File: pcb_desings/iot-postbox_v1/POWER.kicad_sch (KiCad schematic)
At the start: 32 parts, among them J1 USB_B_Micro, J4 BAT, J5 3V3_LDO2, Q1 AO3401A, U5 MCP73831-2-OT, U6 NCP167BMX330TBG, U7 NCP167BMX330TBG

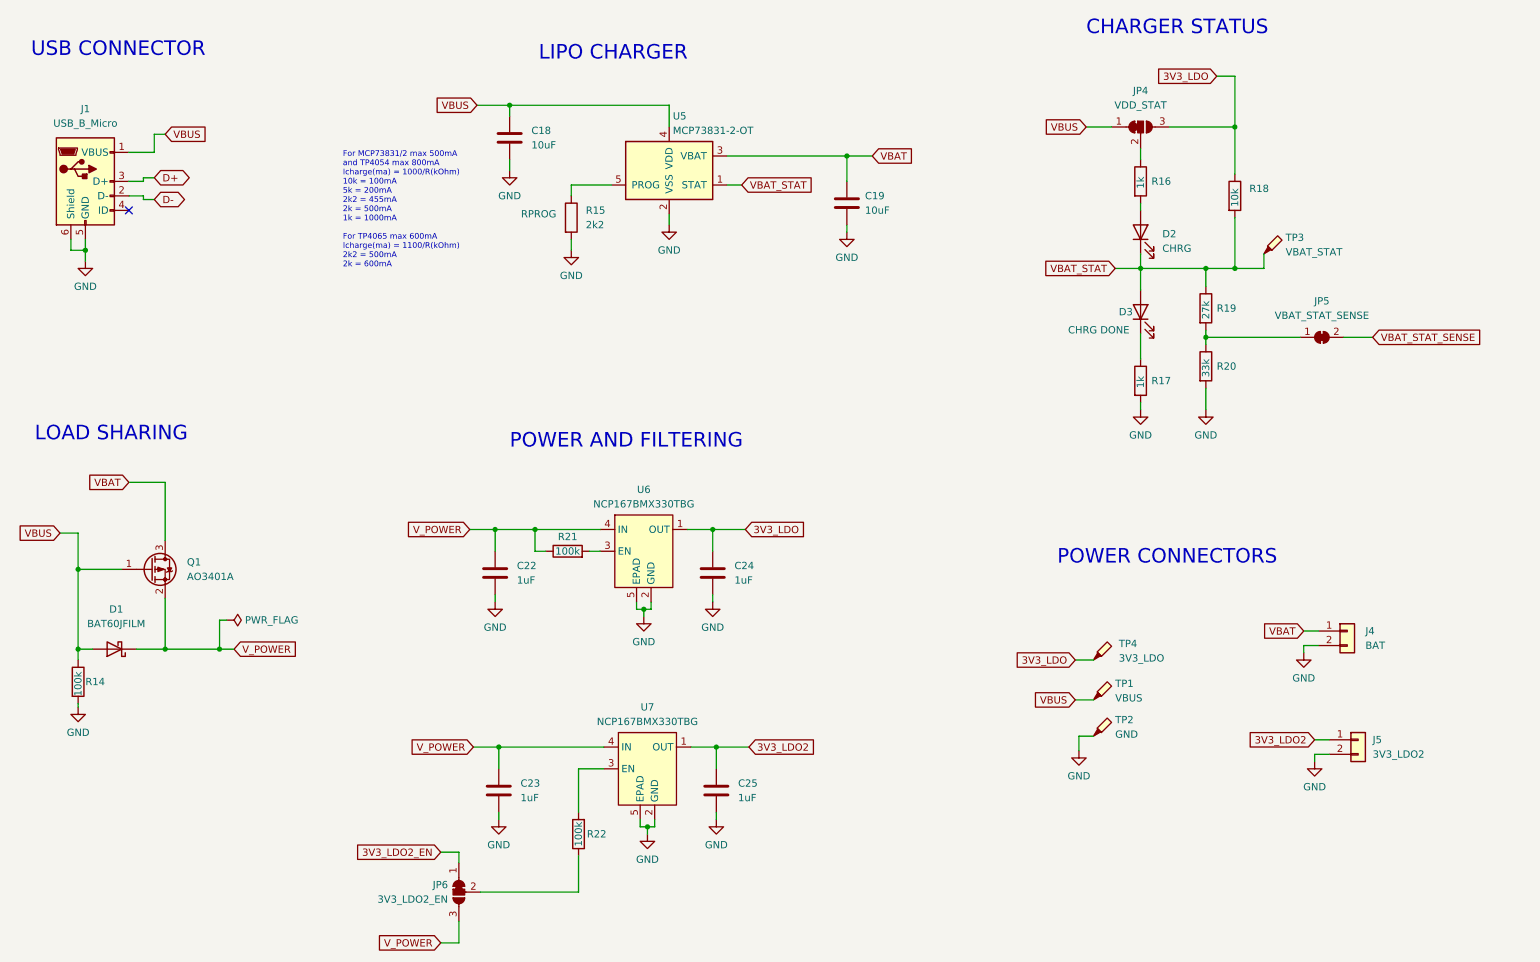
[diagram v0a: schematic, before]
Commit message: Added iot-postbox_v1 sch to v1.1. Added minor documentation
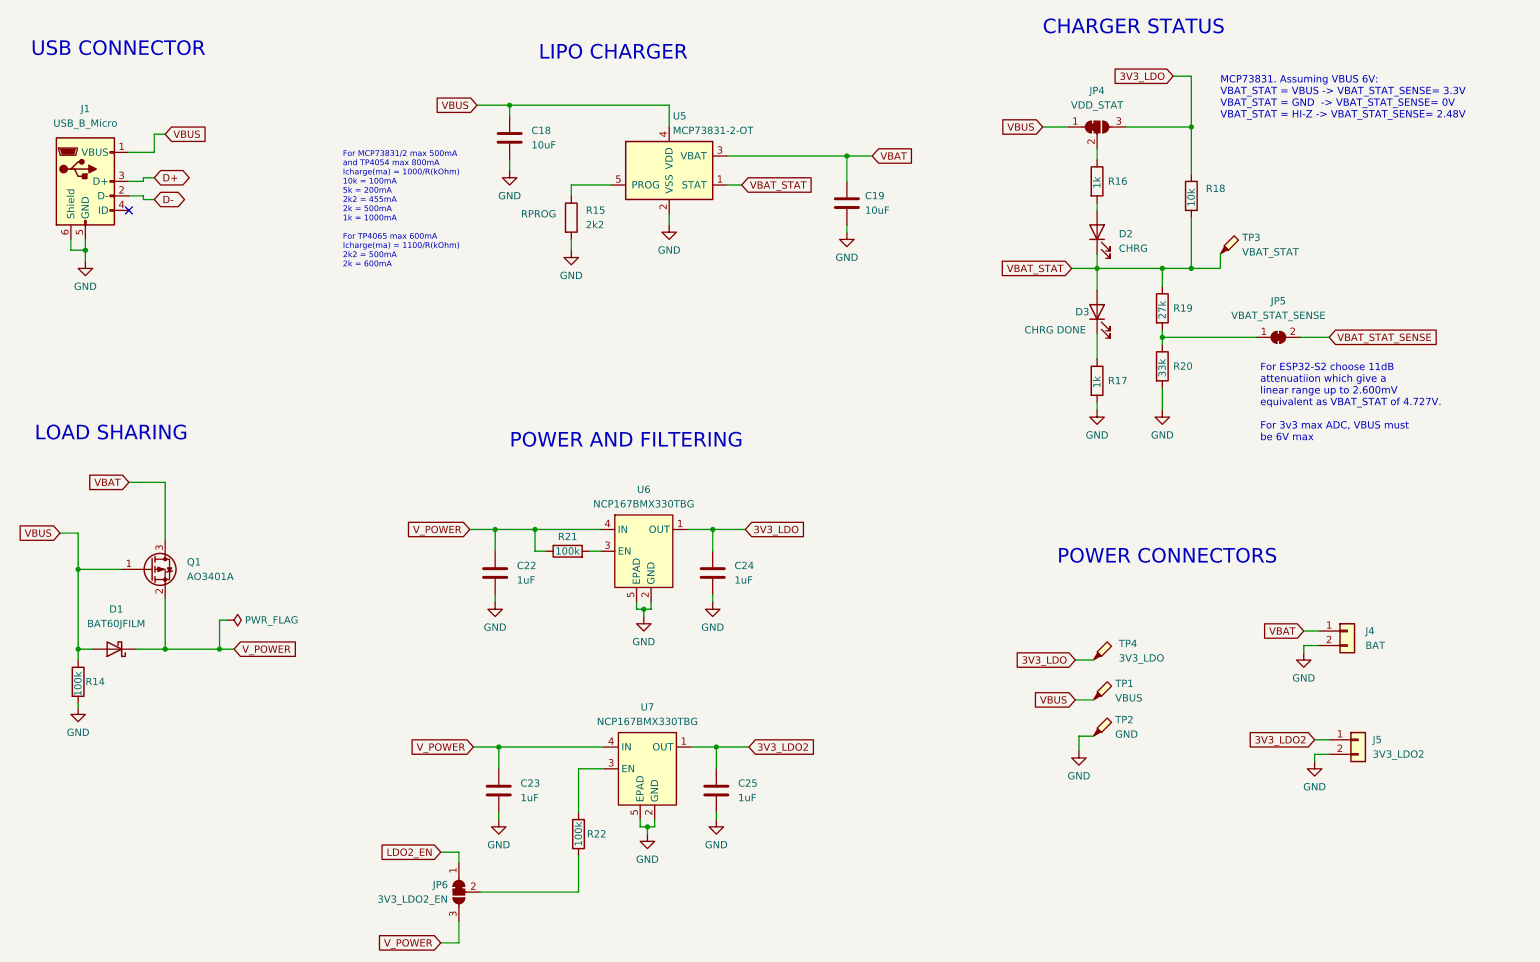
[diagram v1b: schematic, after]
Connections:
- net 3V3_LDO2_EN renamed LDO2_EN
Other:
- note added: "For ESP32-S2 choose 11dB attenuatiion which give a linear range up to 2.600mV equivalent as VBAT_STAT of 4.727V. For 3v3 max ADC, VBUS must be 6V max"
- note added: "MCP73831. Assuming VBUS 6V: VBAT_STAT = VBUS -> VBAT_STAT_SENSE= 3.3V VBAT_STAT = GND -> VBAT_STAT_SENSE= 0V VBAT_STAT = HI-Z -> VBAT_STAT_SENSE= 2.48V"
- moved on the sheet: D2, D3, JP4, JP5, R16, R17, R18, R19, R20, TP3

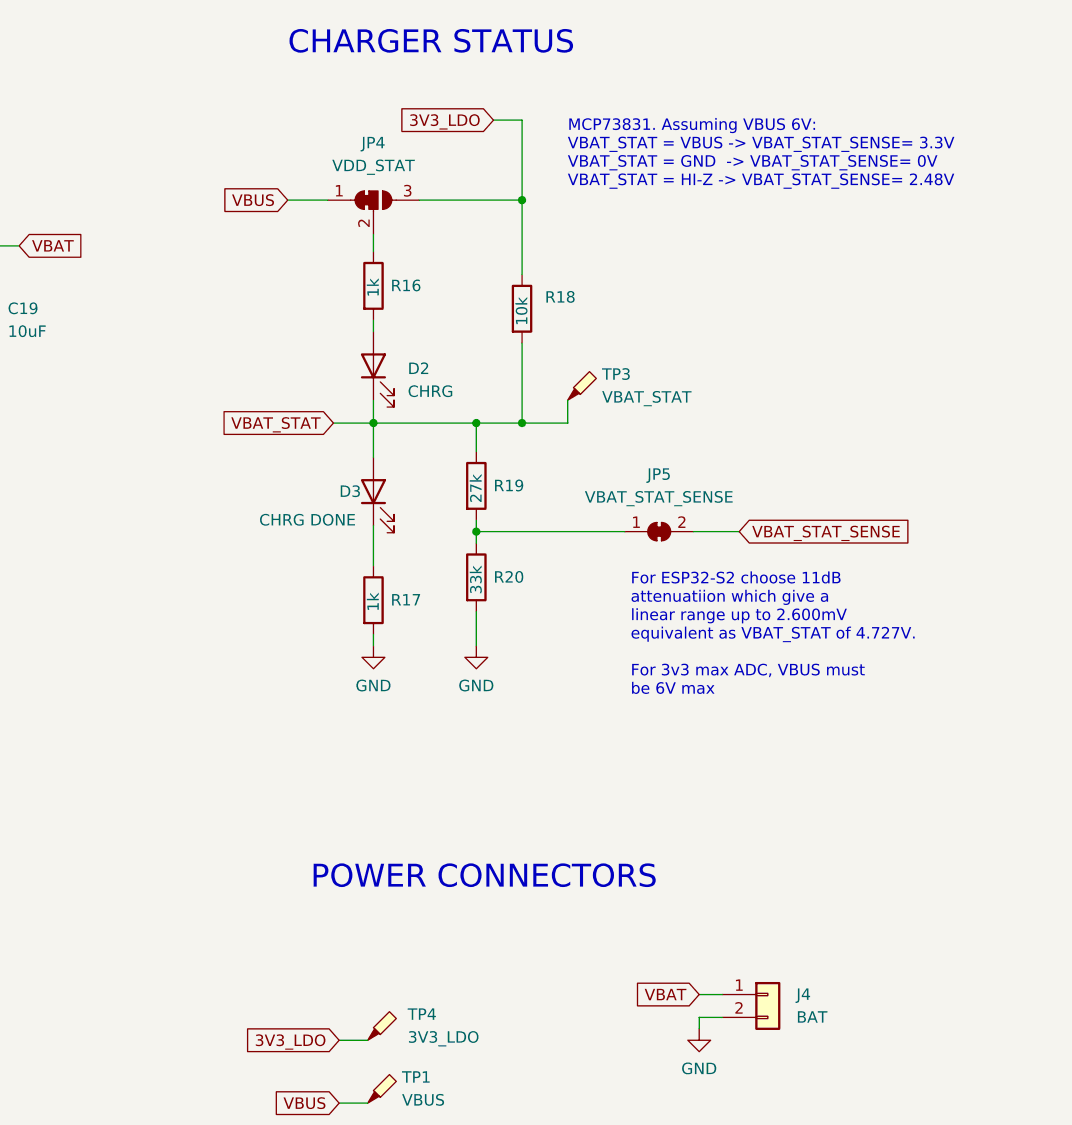
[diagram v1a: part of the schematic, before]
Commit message: Changed led strip instance as fastled object insted adafruit neopixel and fixed power and charging states
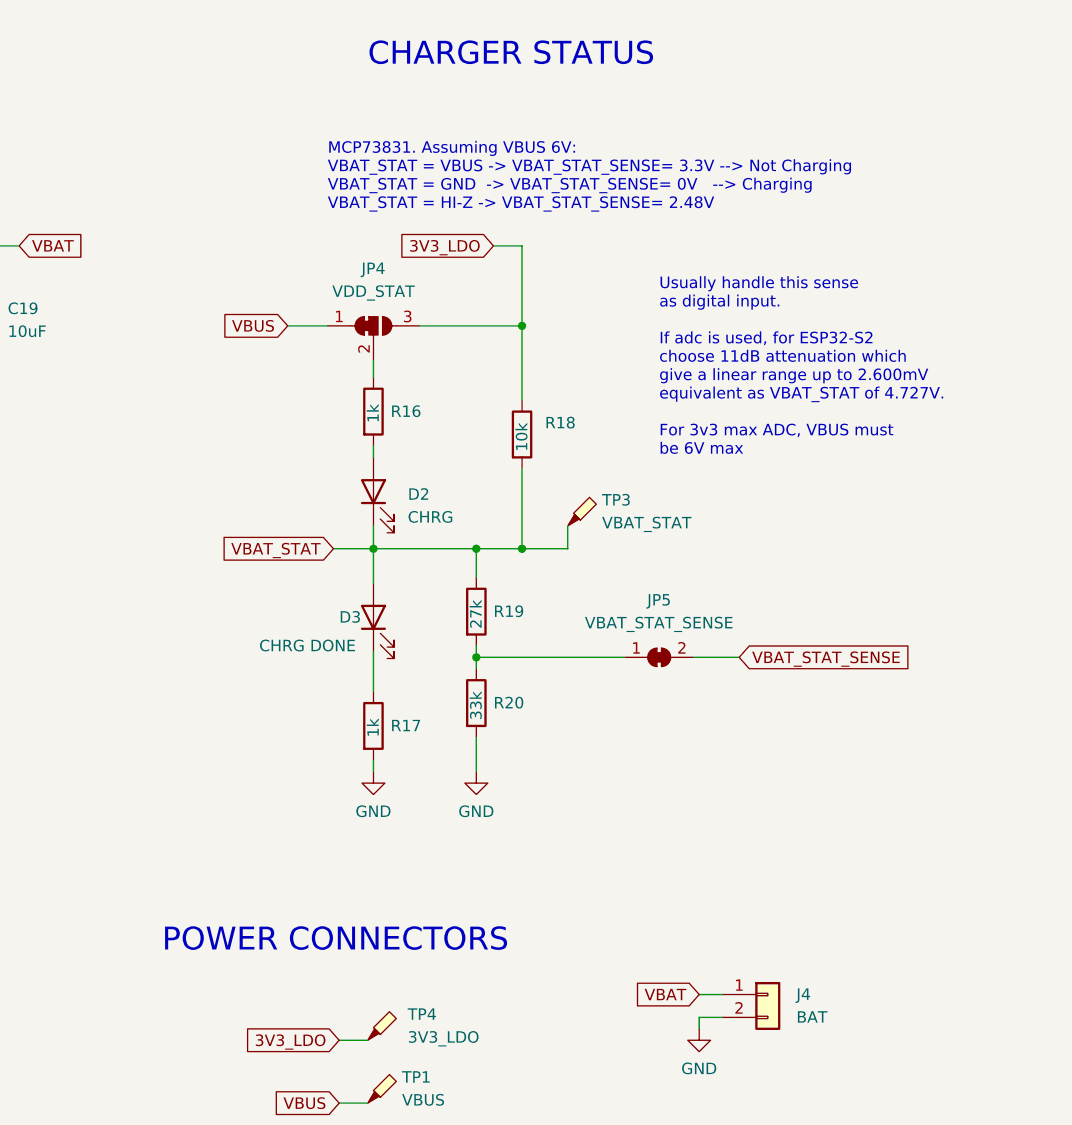
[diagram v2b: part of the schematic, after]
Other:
- note added: "MCP73831. Assuming VBUS 6V: VBAT_STAT = VBUS -> VBAT_STAT_SENSE= 3.3V --> Not Charging VBAT_STAT = GND -> VBAT_STAT_SENSE= 0V --> Charging VBAT_STAT = HI-Z -> VBAT_STAT_SENSE= 2.48V"
- note added: "Usually handle this sense as digital input. If adc is used, for ESP32-S2 choose 11dB attenuation which give a linear range up to 2.600mV equivalent as VBAT_STAT of 4.727V. For 3v3 max ADC, VBUS must be 6V max"
- note removed: "For ESP32-S2 choose 11dB attenuatiion which give a linear range up to 2.600mV equivalent as VBAT_STAT of 4.727V. For 3v3 max ADC, VBUS must be 6V max"
- note removed: "MCP73831. Assuming VBUS 6V: VBAT_STAT = VBUS -> VBAT_STAT_SENSE= 3.3V VBAT_STAT = GND -> VBAT_STAT_SENSE= 0V VBAT_STAT = HI-Z -> VBAT_STAT_SENSE= 2.48V"
- moved on the sheet: D2, D3, JP4, JP5, R16, R17, R18, R19, R20, TP3

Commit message: Added charging circuit test findings
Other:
- note added: "Depending the IC, the VBAT_STAT output can be: - Tri-state output: MCP73831 - Open-drain output: MCP73832, TP4054 or TP4065 Only for Open-drain, R18 make sense because VDD_STAT can be configurable only in that case"
- note added: "For MCP73831/2 max 500mA and TP4054 max 800mA Icharge(ma) = 1000(V)/R(kOhm) 10k = 100mA 5k = 200mA 2k2 = 455mA 2k = 500mA 1k = 1000mA For TP4065 max 600mA Icharge(ma) = 1100/R(kOhm) 2k2 = 500mA 2k = 600mA"
- note removed: "For MCP73831/2 max 500mA and TP4054 max 800mA Icharge(ma) = 1000/R(kOhm) 10k = 100mA 5k = 200mA 2k2 = 455mA 2k = 500mA 1k = 1000mA For TP4065 max 600mA Icharge(ma) = 1100/R(kOhm) 2k2 = 500mA 2k = 600mA"
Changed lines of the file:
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@@
     (effects (font (size 1.27 1.27)) (justify left bottom))
   )
-  (text "For MCP73831/2 max 500mA \nand TP4054 max 800mA\nIcharge(ma) = 1000/R(kOhm)\n10k = 100mA\n5k = 200mA\n2k2 = 455mA\n2k = 500mA\n1k = 1000mA\n\nFor TP4065 max 600mA\nIcharge(ma) = 1100/R(kOhm)\n2k2 = 500mA\n2k = 600mA"
-    (at 80.01 65.405 0)
+  (text "For MCP73831/2 max 500mA \nand TP4054 max 800mA\nIcharge(ma) = 1000(V)/R(kOhm)\n10k = 100mA\n5k = 200mA\n2k2 = 455mA\n2k = 500mA\n1k = 1000mA\n\nFor TP4065 max 600mA\nIcharge(ma) = 1100/R(kOhm)\n2k2 = 500mA\n2k = 600mA"
+    (at 77.47 63.5 0)
     (effects (font (size 1 1)) (justify left bottom))
   )
@@
     (effects (font (size 2.54 2.54)) (justify left bottom))
   )
+  (text "Depending the IC, the VBAT_STAT output can be:\n- Tri-state output: MCP73831\n- Open-drain output: MCP73832, TP4054 or TP4065\nOnly for Open-drain, R18 make sense because \nVDD_STAT can be configurable only in that case"
+    (at 139.7 74.295 0)
+    (effects (font (size 1 1)) (justify left bottom))
+  )
   (text "LIPO CHARGER" (at 114.3 29.21 0)
     (effects (font (size 2.54 2.54)) (justify left bottom))
   )
   (text "MCP73831. Assuming VBUS 6V:\nVBAT_STAT = VBUS -> VBAT_STAT_SENSE= 3.3V --> Not Charging\nVBAT_STAT = GND  -> VBAT_STAT_SENSE= 0V   --> Charging\nVBAT_STAT = HI-Z -> VBAT_STAT_SENSE= 2.48V"
-    (at 207.01 41.91 0)
+    (at 201.93 40.64 0)
     (effects (font (size 1.27 1.27)) (justify left bottom))
   )

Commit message: Added some sch info
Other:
- note added: "Protecctions: - Battery and input reverse polarity WARNING: - No temp protection - No Overcurrent protection"
- note added: "Usually handle VBAT_STAT_SENSE as digital input. If ADC is used, for ESP32-S2 choose 11dB attenuation which give a linear range up to 2.600mV equivalent as VBAT_STAT of 4.727V. For 3v3 max ADC, VBUS must be 6V max"
- note removed: "Usually handle this sense as digital input. If adc is used, for ESP32-S2 choose 11dB attenuation which give a linear range up to 2.600mV equivalent as VBAT_STAT of 4.727V. For 3v3 max ADC, VBUS must be 6V max"
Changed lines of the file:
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@@
     (effects (font (size 2.54 2.54)) (justify left bottom))
   )
-  (text "Usually handle this sense \nas digital input.\n\nIf adc is used, for ESP32-S2 \nchoose 11dB attenuation which \ngive a linear range up to 2.600mV\nequivalent as VBAT_STAT of 4.727V.\n\nFor 3v3 max ADC, VBUS must\nbe 6V max "
+  (text "Usually handle VBAT_STAT_SENSE \nas digital input.\n\nIf ADC is used, for ESP32-S2 \nchoose 11dB attenuation which \ngive a linear range up to 2.600mV\nequivalent as VBAT_STAT of 4.727V.\n\nFor 3v3 max ADC, VBUS must\nbe 6V max "
     (at 243.84 69.215 0)
     (effects (font (size 1.27 1.27)) (justify left bottom))
@@
     (effects (font (size 2.54 2.54)) (justify left bottom))
   )
+  (text "Protecctions:\n- Battery and input reverse polarity\nWARNING:\n- No temp protection\n- No Overcurrent protection"
+    (at 151.13 34.29 0)
+    (effects (font (size 1 1)) (justify left bottom))
+  )
   (text "MCP73831. Assuming VBUS 6V:\nVBAT_STAT = VBUS -> VBAT_STAT_SENSE= 3.3V --> Not Charging\nVBAT_STAT = GND  -> VBAT_STAT_SENSE= 0V   --> Charging\nVBAT_STAT = HI-Z -> VBAT_STAT_SENSE= 2.48V"

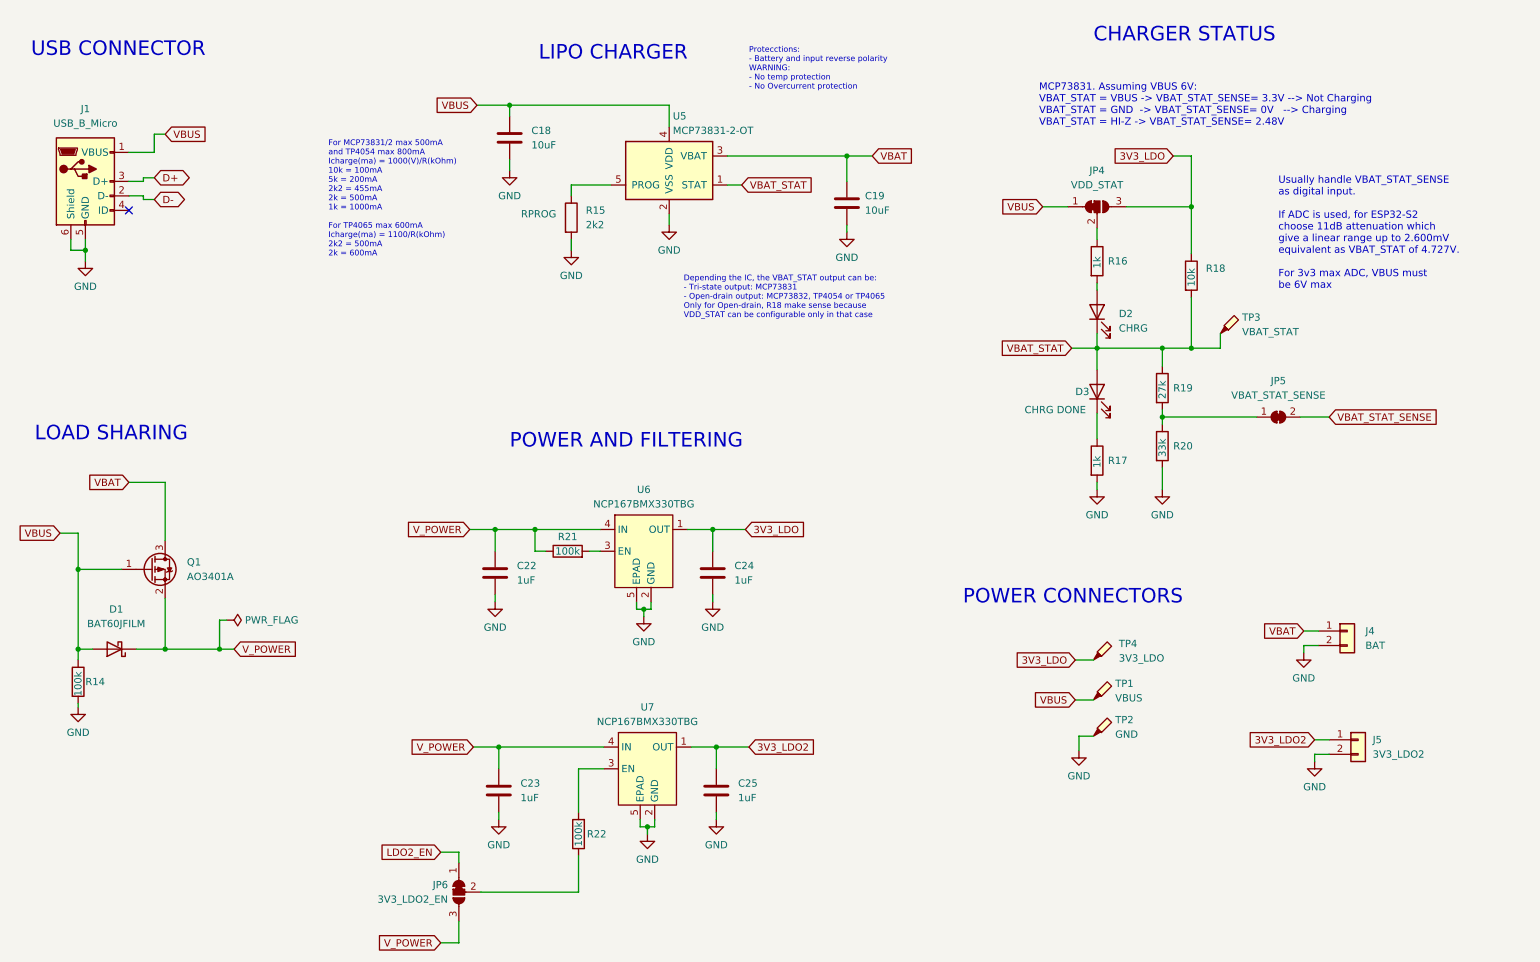
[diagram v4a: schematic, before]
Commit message: Created iot-postbox v1.2 migrating to kicad v9. Fixed missing 3d designs, replaced horizontal footprints for some connectors.
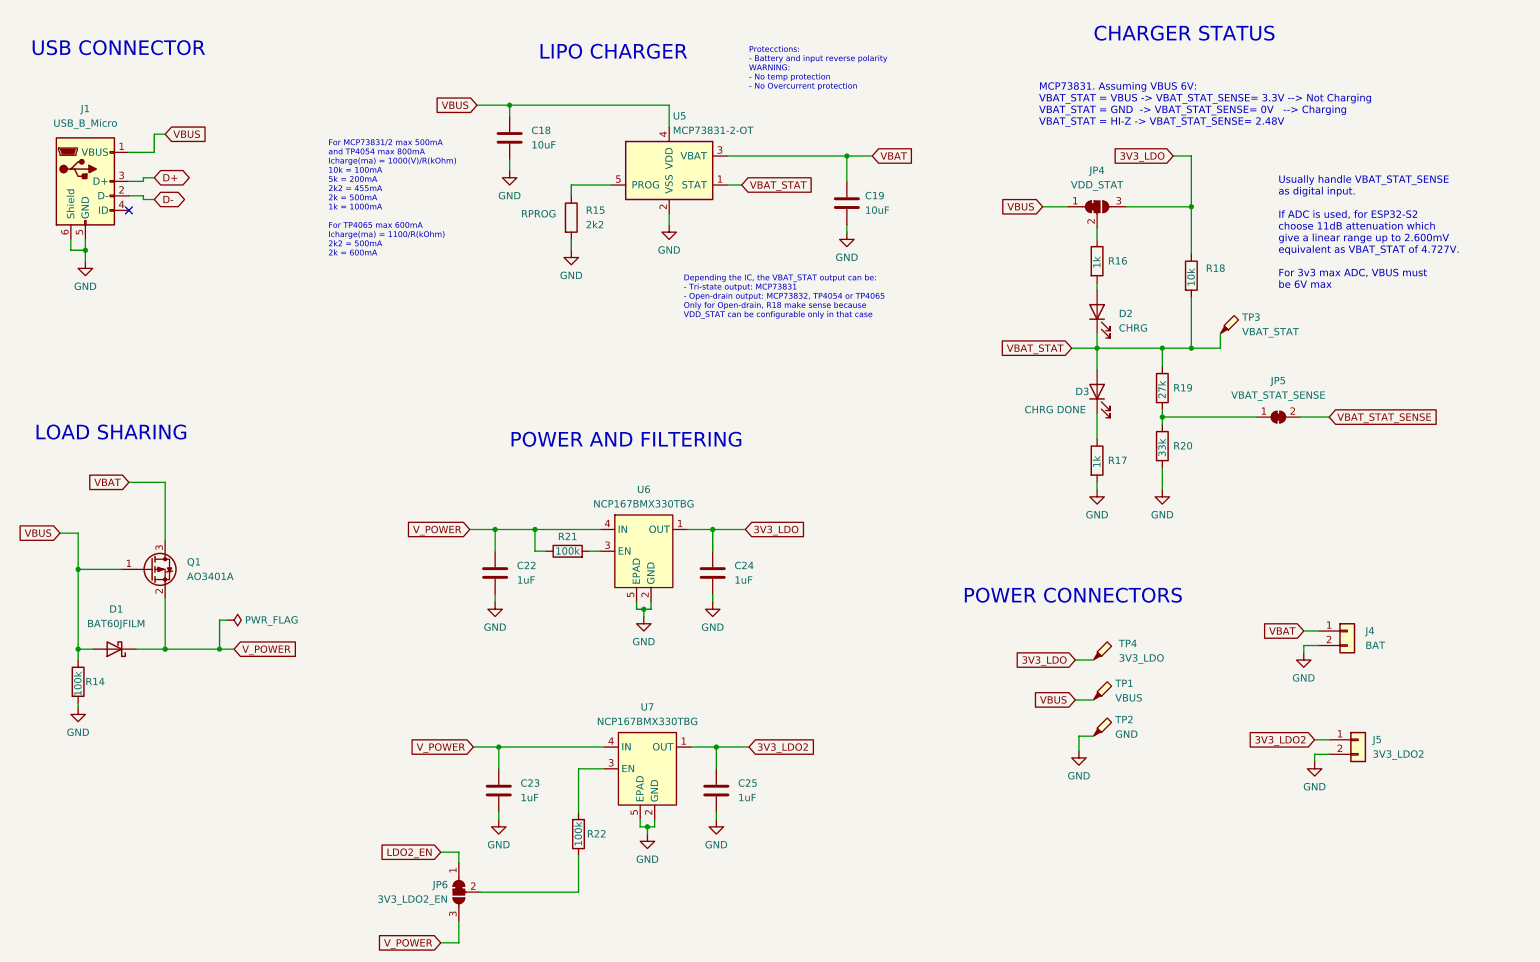
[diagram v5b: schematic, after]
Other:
- company: (none) -> @paclema
